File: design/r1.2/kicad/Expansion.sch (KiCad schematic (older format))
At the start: 28 parts, among them IC1 MC68010P10, IC4 MC68901P, IC6 74174N, IC9 74LS01N, J1 PWR, J3 Conn_02x32_Odd_Even, J5 GPIO-PANEL

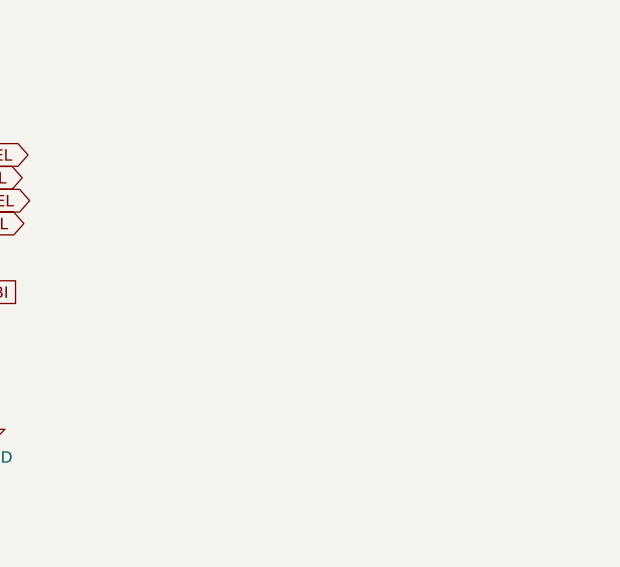
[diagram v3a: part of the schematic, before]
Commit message: Tidy up IO and add SPI header, roll r1.22
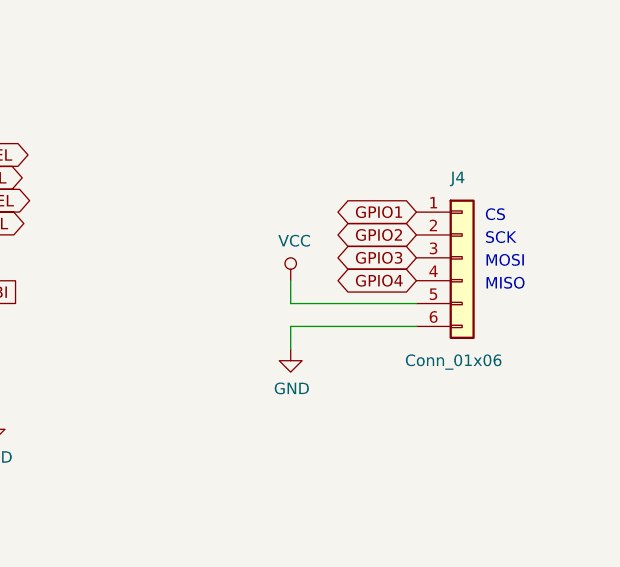
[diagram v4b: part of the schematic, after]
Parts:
- added J4: Conn_01x06, rosco_m68k:1X06, symbol Connector_Generic:Conn_01x06
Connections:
- net GND: now also J4.6 (Pin_6)
- net GPIO1: now also J4.1 (Pin_1)
- net GPIO2: now also J4.2 (Pin_2)
- net GPIO3: now also J4.3 (Pin_3)
- net GPIO4: now also J4.4 (Pin_4)
- net VCC: now also J4.5 (Pin_5)
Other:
- note added: "CS"
- note added: "MISO"
- note added: "MOSI"
- note added: "SCK"
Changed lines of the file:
@@
 Sheet 4 4
 Title "EXPANSION AND MECHANICAL"
-Date "2020-05-26"
-Rev "1.2"
-Comp ""
+Date "2021-03-05"
+Rev "1.22"
+Comp "The Really Old-School Company Limited"
 Comment1 "OSHWA UK000006 (https://certification.oshwa.org/uk000006.html)"
 Comment2 "See https://github.com/roscopeco/rosco_m68k/blob/master/LICENCE.hardware.txt"
 Comment3 "Open Source Hardware licenced under CERN Open Hardware Licence"
-Comment4 "Copyright 2019-2020 Ross Bamford and Contributors"
+Comment4 "Copyright 2019-2021 Ross Bamford and Contributors"
 $EndDescr
 Wire Wire Line
@@
 Wire Wire Line
 	10950 7400 10950 7850
+$Comp
+L Connector_Generic:Conn_01x06 J?
+U 1 1 60465FFE
+P 13000 7150
+AR Path="/5E53B4B8/60465FFE" Ref="J?"  Part="1"
+AR Path="/5E53BC83/60465FFE" Ref="J4"  Part="1"
+F 0 "J4" H 12950 7500 50  0000 L CNN
+F 1 "Conn_01x06" H 12750 6700 50  0000 L CNN
+F 2 "rosco_m68k:1X06" H 13000 7150 50  0001 C CNN
+F 3 "~" H 13000 7150 50  0001 C CNN
+	1    13000 7150
+	1    0    0    -1
+$EndComp
+Text GLabel 12800 6950 0    50   BiDi ~ 0
+GPIO1
+Text Notes 13100 7000 0    50   ~ 0
+CS
+Text Notes 13100 7100 0    50   ~ 0
+SCK
+Text GLabel 12800 7050 0    50   BiDi ~ 0
+GPIO2
+Text GLabel 12800 7150 0    50   BiDi ~ 0
+GPIO3
+Text GLabel 12800 7250 0    50   BiDi ~ 0
+GPIO4
+Text Notes 13100 7200 0    50   ~ 0
+MOSI
+Text Notes 13100 7300 0    50   ~ 0
+MISO
+$Comp
+L power:VCC #PWR0129
+U 1 1 604703CB
+P 12250 7250
+F 0 "#PWR0129" H 12250 7100 50  0001 C CNN
+F 1 "VCC" H 12267 7423 50  0000 C CNN
+F 2 "" H 12250 7250 50  0001 C CNN
+F 3 "" H 12250 7250 50  0001 C CNN
+	1    12250 7250
+	1    0    0    -1
+$EndComp
+$Comp
+L power:GND #PWR0130
+U 1 1 60470D8A
+P 12250 7550
+F 0 "#PWR0130" H 12250 7300 50  0001 C CNN
+F 1 "GND" H 12255 7377 50  0000 C CNN
+F 2 "" H 12250 7550 50  0001 C CNN
+F 3 "" H 12250 7550 50  0001 C CNN
+	1    12250 7550
+	1    0    0    -1
+$EndComp
+Wire Wire Line
+	12800 7350 12250 7350
+Wire Wire Line
+	12250 7350 12250 7250
+Wire Wire Line
+	12800 7450 12250 7450
+Wire Wire Line
+	12250 7450 12250 7550
 Wire Bus Line
 	11150 4100 11150 5700

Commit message: Revert "Merge pull request #181 from rosco-m68k/feature/board-1.22"
This reverts commit 67e3259ef153c8a657db8d826cd60eea2d9b52e3, reversing
changes made to 43bb90592578d0b0c5d0a3f828a55b4324962c1a.
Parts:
- removed J4: Conn_01x06, rosco_m68k:1X06, symbol Connector_Generic:Conn_01x06
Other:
- note removed: "CS"
- note removed: "MISO"
- note removed: "MOSI"
- note removed: "SCK"
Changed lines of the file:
@@
 Sheet 4 4
 Title "EXPANSION AND MECHANICAL"
-Date "2021-03-05"
-Rev "1.22"
-Comp "The Really Old-School Company Limited"
+Date "2020-05-26"
+Rev "1.2"
+Comp ""
 Comment1 "OSHWA UK000006 (https://certification.oshwa.org/uk000006.html)"
 Comment2 "See https://github.com/roscopeco/rosco_m68k/blob/master/LICENCE.hardware.txt"
 Comment3 "Open Source Hardware licenced under CERN Open Hardware Licence"
-Comment4 "Copyright 2019-2021 Ross Bamford and Contributors"
+Comment4 "Copyright 2019-2020 Ross Bamford and Contributors"
 $EndDescr
 Wire Wire Line
@@
 Wire Wire Line
 	10950 7400 10950 7850
-$Comp
-L Connector_Generic:Conn_01x06 J?
-U 1 1 60465FFE
-P 13000 7150
-AR Path="/5E53B4B8/60465FFE" Ref="J?"  Part="1"
-AR Path="/5E53BC83/60465FFE" Ref="J4"  Part="1"
-F 0 "J4" H 12950 7500 50  0000 L CNN
-F 1 "Conn_01x06" H 12750 6700 50  0000 L CNN
-F 2 "rosco_m68k:1X06" H 13000 7150 50  0001 C CNN
-F 3 "~" H 13000 7150 50  0001 C CNN
-	1    13000 7150
-	1    0    0    -1
-$EndComp
-Text GLabel 12800 6950 0    50   BiDi ~ 0
-GPIO1
-Text Notes 13100 7000 0    50   ~ 0
-CS
-Text Notes 13100 7100 0    50   ~ 0
-SCK
-Text GLabel 12800 7050 0    50   BiDi ~ 0
-GPIO2
-Text GLabel 12800 7150 0    50   BiDi ~ 0
-GPIO3
-Text GLabel 12800 7250 0    50   BiDi ~ 0
-GPIO4
-Text Notes 13100 7200 0    50   ~ 0
-MOSI
-Text Notes 13100 7300 0    50   ~ 0
-MISO
-$Comp
-L power:VCC #PWR0129
-U 1 1 604703CB
-P 12250 7250
-F 0 "#PWR0129" H 12250 7100 50  0001 C CNN
-F 1 "VCC" H 12267 7423 50  0000 C CNN
-F 2 "" H 12250 7250 50  0001 C CNN
-F 3 "" H 12250 7250 50  0001 C CNN
-	1    12250 7250
-	1    0    0    -1
-$EndComp
-$Comp
-L power:GND #PWR0130
-U 1 1 60470D8A
-P 12250 7550
-F 0 "#PWR0130" H 12250 7300 50  0001 C CNN
-F 1 "GND" H 12255 7377 50  0000 C CNN
-F 2 "" H 12250 7550 50  0001 C CNN
-F 3 "" H 12250 7550 50  0001 C CNN
-	1    12250 7550
-	1    0    0    -1
-$EndComp
-Wire Wire Line
-	12800 7350 12250 7350
-Wire Wire Line
-	12250 7350 12250 7250
-Wire Wire Line
-	12800 7450 12250 7450
-Wire Wire Line
-	12250 7450 12250 7550
 Wire Bus Line
 	11150 4100 11150 5700
